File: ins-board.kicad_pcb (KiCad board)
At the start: 2 copper layers, 35 x 20 mm, 48 parts, among them P1 CONN_8, P2 PWR, U1 STM32F042C6T6, U2 MIC5201-3.3YS, U3 H3LIS331DL, U4 MPU6000, U5 LPS331AP, X1 CRYSTAL 16MHz 10ppm

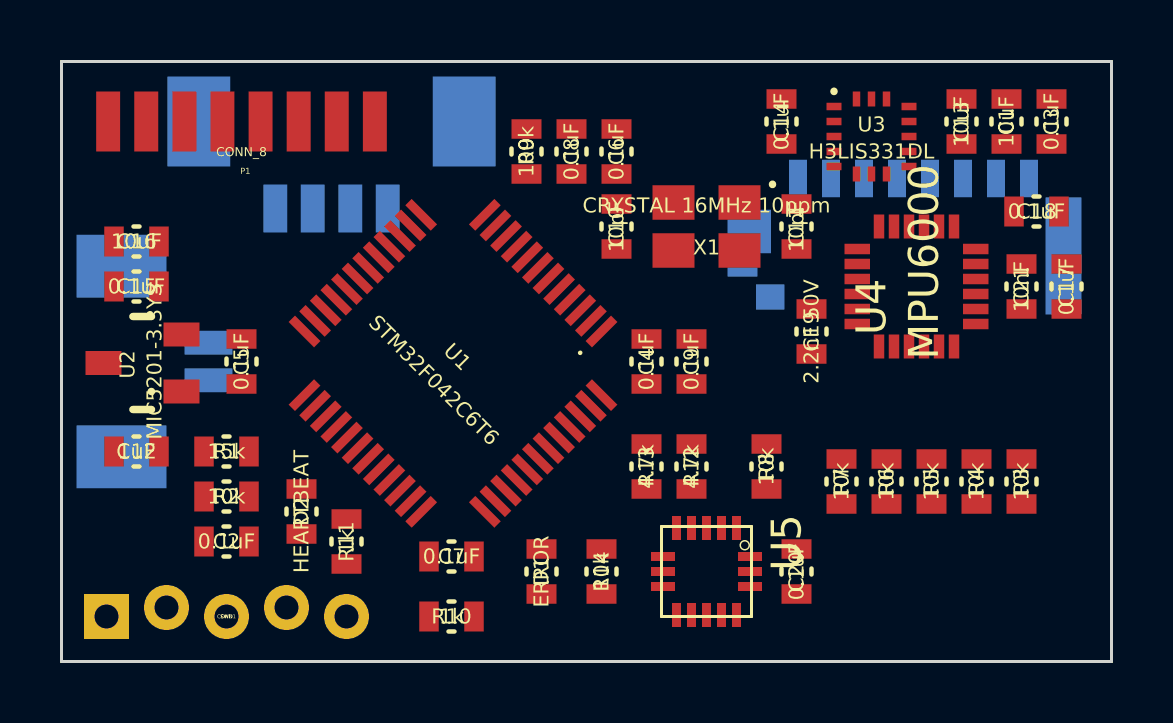
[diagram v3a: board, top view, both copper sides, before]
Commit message: Replace components to ease routing
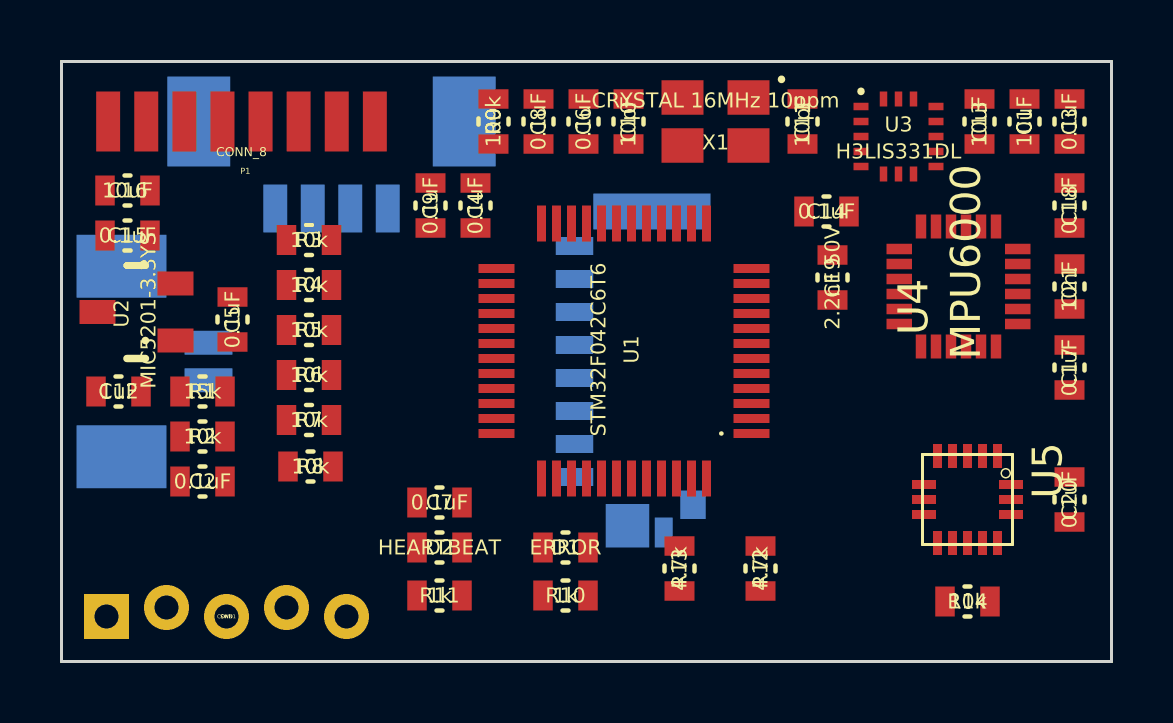
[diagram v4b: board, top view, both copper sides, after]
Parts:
- moved R3 25.1 mm to (141.2, 93.5), turned to 0 degrees
- moved R4 23.2 mm to (141.2, 95.0), turned to 0 degrees
- moved R5 21.4 mm to (141.2, 96.5), turned to 0 degrees
- moved R6 19.6 mm to (141.2, 98.0), turned to 0 degrees
- moved R7 17.9 mm to (141.2, 99.5), turned to 0 degrees
- moved R8 15.2 mm to (141.3, 101.0), turned to 0 degrees
- moved CONN2 12.8 mm to (150.1, 97.5), turned to 270 degrees
- moved R14 12.2 mm to (163.2, 105.5), turned to 180 degrees
- moved C9 10.1 mm to (145.3, 92.3), turned to 90 degrees
- moved C20 9.41 mm to (166.6, 102.1)
- moved U5 9.02 mm to (164.7, 100.6)
- moved C4 7.72 mm to (146.8, 92.3), turned to 90 degrees
- moved U1 6.05 mm to (156.0, 99.9), turned to 90 degrees
- moved D2 4.75 mm to (145.6, 103.7), turned to 180 degrees
- moved R12 4.10 mm to (156.3, 104.4)
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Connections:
- P1 pad 1: VCC -> Net-(P1-Pad1)
- P1 pad 2: GND -> Net-(P1-Pad2)
- P1 pad 7: Net-(P1-Pad7) -> VCC
- P1 pad 8: Net-(P1-Pad8) -> GND
- U1 pad 10: (no net) -> Net-(U1-Pad10)
- U1 pad 12: Net-(P1-Pad3) -> Net-(P1-Pad1)
- U1 pad 13: Net-(P1-Pad4) -> Net-(P1-Pad2)
- U1 pad 14: Net-(P1-Pad5) -> Net-(P1-Pad3)
- U1 pad 15: Net-(P1-Pad6) -> Net-(P1-Pad4)
- U1 pad 16: Net-(P1-Pad7) -> Net-(P1-Pad5)
- U1 pad 17: Net-(P1-Pad8) -> Net-(P1-Pad6)
- U1 pad 18: (no net) -> Net-(U1-Pad18)
- U1 pad 2: (no net) -> Net-(U1-Pad2)
- U1 pad 21: (no net) -> Net-(U1-Pad21)
- U1 pad 22: (no net) -> Net-(U1-Pad22)
- U1 pad 3: (no net) -> Net-(U1-Pad3)
- U1 pad 32: (no net) -> Net-(U1-Pad32)
- U1 pad 33: (no net) -> Net-(U1-Pad33)
- U1 pad 4: (no net) -> Net-(U1-Pad4)
- U1 pad 40: (no net) -> Net-(U1-Pad40)
- U1 pad 41: (no net) -> Net-(U1-Pad41)
- U1 pad 45: (no net) -> Net-(U1-Pad45)
- U1 pad 46: (no net) -> Net-(U1-Pad46)
- U3 pad 9: (no net) -> Net-(U3-Pad9)
- U4 pad 22: (no net) -> Net-(U4-Pad22)
- U4 pad 6: (no net) -> Net-(U4-Pad6)
- U4 pad 7: (no net) -> Net-(U4-Pad7)
- U5 pad 11: (no net) -> Net-(U5-Pad11)
- U5 pad 2: (no net) -> Net-(U5-Pad2)
- U5 pad 3: (no net) -> Net-(U5-Pad3)
- U5 pad 9: (no net) -> Net-(U5-Pad9)

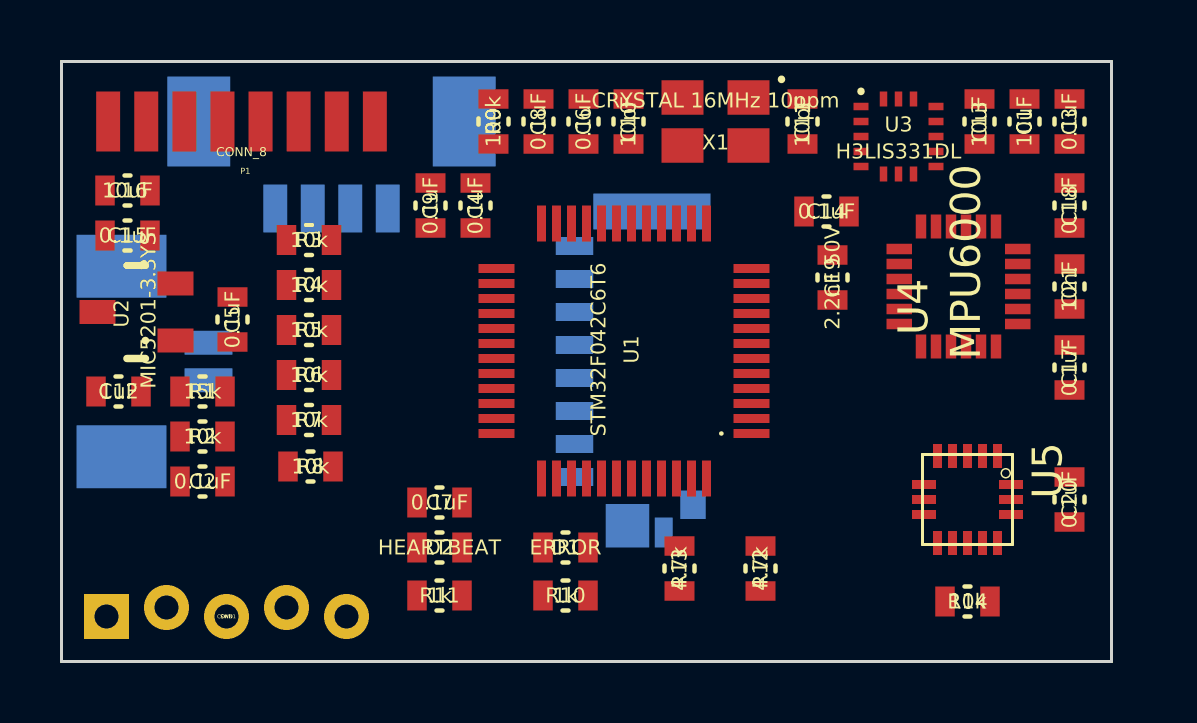
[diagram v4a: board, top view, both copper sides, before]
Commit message: Replace components to ease routing (2)
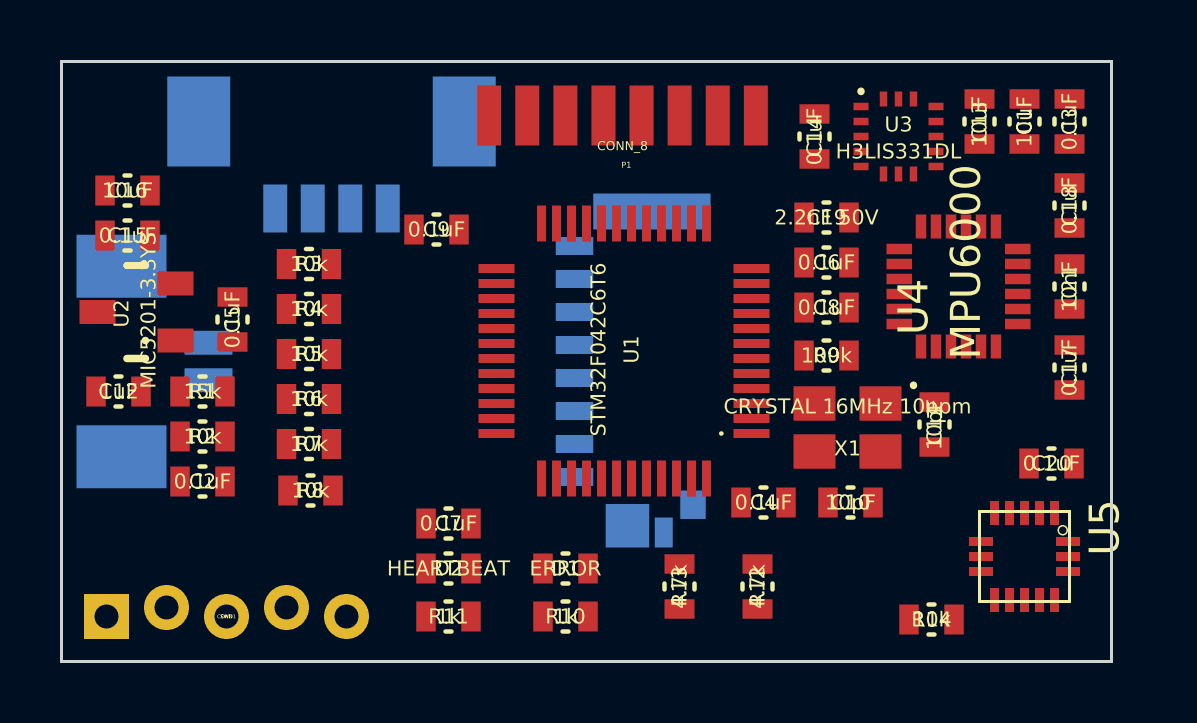
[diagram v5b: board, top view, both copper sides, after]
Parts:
- moved C10 14.7 mm to (159.3, 102.2), turned to 0 degrees
- moved C4 13.8 mm to (156.4, 102.2), turned to 180 degrees
- moved R9 13.6 mm to (158.5, 97.3), turned to 0 degrees
- moved P1 12.7 mm to (151.7, 89.3)
- moved C8 11.4 mm to (158.5, 95.7), turned to 0 degrees
- moved X1 11.1 mm to (159.2, 99.7)
- moved C11 11.0 mm to (162.1, 99.6)
- moved C6 9.36 mm to (158.5, 94.2), turned to 0 degrees
- moved U5 2.69 mm to (166.6, 102.5)
- moved C14 2.53 mm to (158.1, 90.0), turned to 270 degrees
- moved C19 2.01 mm to (158.5, 92.7), turned to 180 degrees
- moved C20 1.34 mm to (166.0, 100.9), turned to 0 degrees
- moved R14 1.34 mm to (162.0, 106.1), turned to 0 degrees
- moved C9 0.82 mm to (145.5, 93.1), turned to 180 degrees
- moved R3 0.80 mm to (141.2, 94.2)
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
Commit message: Routing
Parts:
- moved C5 20.2 mm to (158.8, 94.0), turned to 0 degrees
- moved C2 13.6 mm to (144.1, 89.5), turned to 270 degrees
- moved R2 11.6 mm to (142.6, 89.5), turned to 270 degrees
- moved C12 10.2 mm to (139.6, 89.5), turned to 270 degrees
- moved R1 9.62 mm to (141.1, 89.5), turned to 90 degrees
- moved U2 5.30 mm to (136.6, 91.5), turned to 270 degrees
- moved C19 4.72 mm to (163.2, 93.1), turned to 90 degrees
- moved R7 4.35 mm to (141.4, 95.9)
- moved U4 3.83 mm to (166.6, 96.0)
- moved C15 3.72 mm to (137.1, 96.5), turned to 0 degrees
- moved C16 3.72 mm to (137.1, 95.0), turned to 0 degrees
- moved C21 3.19 mm to (168.3, 92.3), turned to 0 degrees
- moved R4 3.15 mm to (141.4, 98.9)
- moved P2 2.39 mm to (136.3, 99.5)
- moved C1 2.31 mm to (167.4, 89.7)
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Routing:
- net GND: track 0.00 -> 227.3 mm, vias 0 -> 8
- net VCC: track 0.00 -> 215.9 mm, vias 0 -> 5
- net /INT_I2C_SCL: track 0.00 -> 48.3 mm, vias 0 -> 4
- net /STM32F4_NRST: track 0.00 -> 33.1 mm, vias 0 -> 1
- net /INT_I2C_SDA: track 0.00 -> 33.0 mm
- net /MPU6000_INT: track 0.00 -> 26.4 mm, vias 0 -> 2
- net /V_BAT_MON_AD: track 0.00 -> 20.7 mm
- net /UART_RX: track 0.00 -> 19.3 mm, vias 0 -> 1
- net /SD_CS: track 0.00 -> 19.3 mm, vias 0 -> 1
- net /H3LIS331DL_INT1: track 0.00 -> 18.8 mm, vias 0 -> 2
- net /UART_TX: track 0.00 -> 17.5 mm, vias 0 -> 1
- net /SD_DIN: track 0.00 -> 15.1 mm, vias 0 -> 1
- net /V_DC: track 0.00 -> 14.1 mm, vias 0 -> 1
- net /SD_CLK: track 0.00 -> 14.0 mm, vias 0 -> 1
- net /STM32F4_SWCLK: track 0.00 -> 13.5 mm
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- added copper zone on B.Cu, net GND
- added copper zone on F.Cu, net GND
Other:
- board size 35 x 20 mm -> 36 x 20 mm
- net class Default: trace_width 0.25 -> 0.2
- net class Power added: clearance 0.2, trace_width 0.3, via_dia 1, via_drill 0.5

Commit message: PCB review + corrections
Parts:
- C1, C3: moved to B.Cu
- moved C1 24.1 mm to (144.6, 97.4), turned to 90 degrees
- moved C3 23.1 mm to (147.2, 97.4), turned to 90 degrees
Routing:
- net VCC: track 215.9 -> 221.8 mm
- net GND: track 227.3 -> 225.6 mm, vias 8 -> 9
- net /STM32F4_NRST: track 33.1 -> 33.4 mm, vias 1 -> 2

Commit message: missing Vcc connection
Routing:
- net VCC: track 221.8 -> 224.6 mm
